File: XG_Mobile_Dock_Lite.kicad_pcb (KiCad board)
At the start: 4 copper layers, 220 x 65 mm, 45 parts, among them J1 5-1775443-8, J10 SWD, J11 UART, J12 I2C1, J13 39300240, J14 469911008, J15 Conn_01x02, J17 8730, J2 20455-040E-76, J3 20455-040E-76, J4 3-2362375-4, J5 USB_C_Receptacle, SW1 SW_Push, U12 STM32F030C8Tx

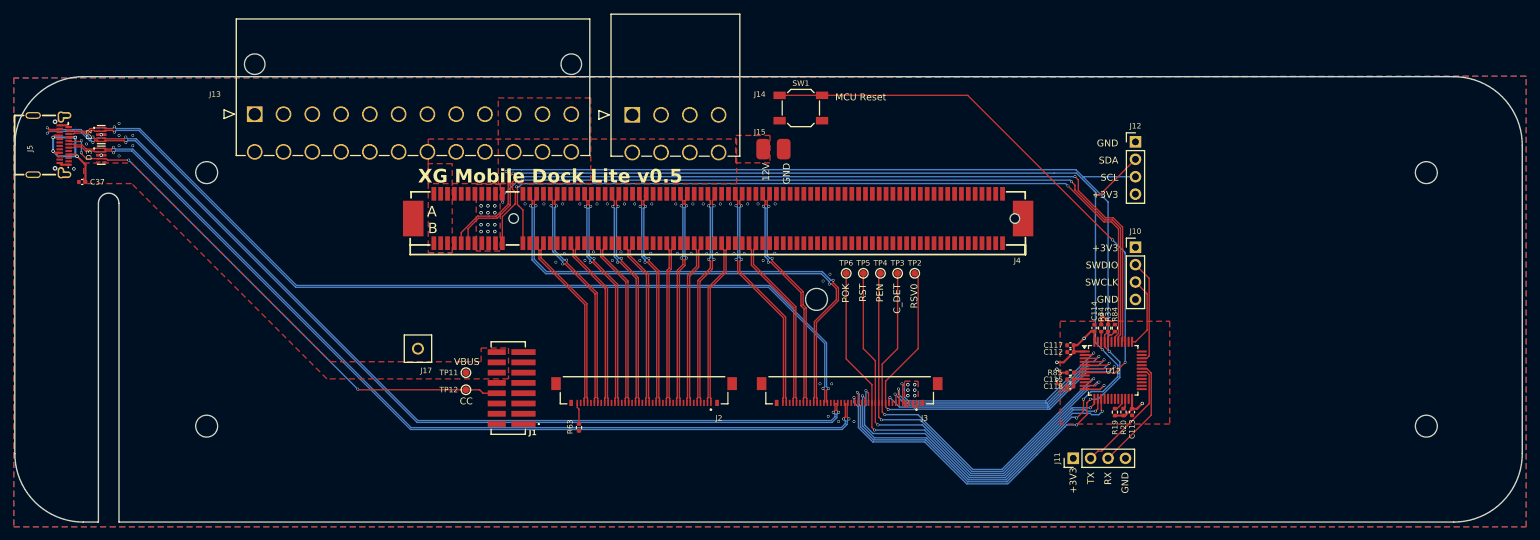
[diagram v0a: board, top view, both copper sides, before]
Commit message: pcb: add pwm fans to lite board
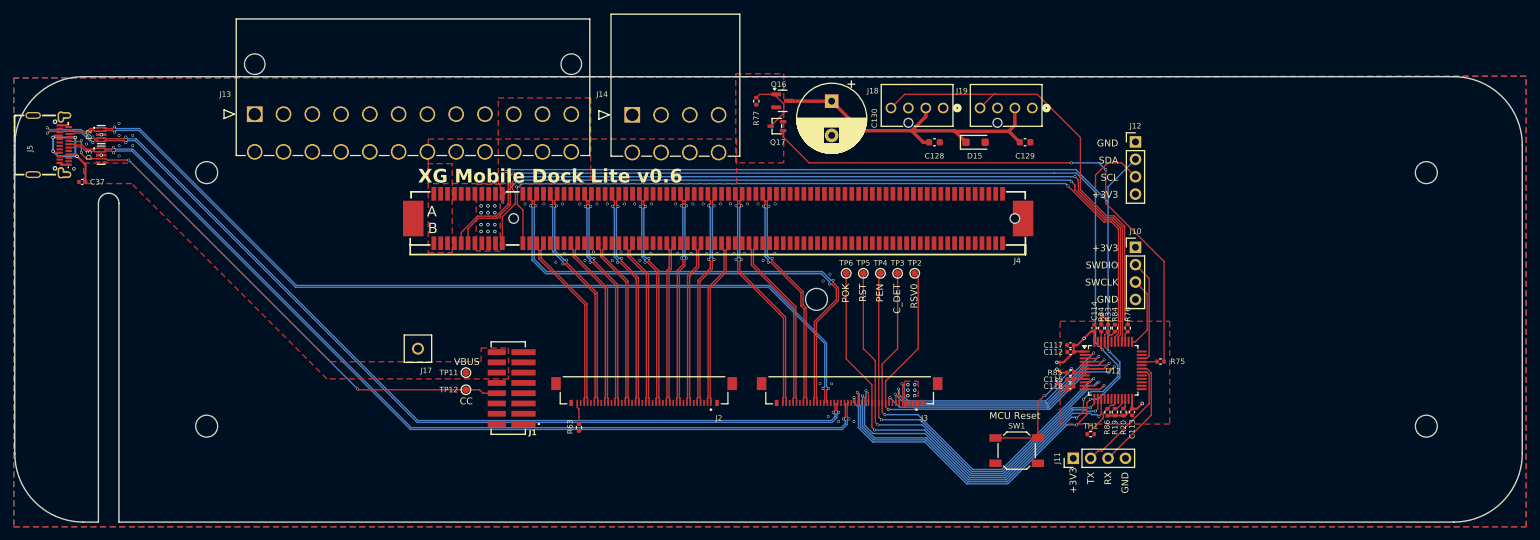
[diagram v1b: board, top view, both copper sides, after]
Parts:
- removed J15: Conn_01x02, XG_Mobile:Solder_Pad_2P
- added C128: 0.1µF, Capacitor_SMD:C_0603_1608Metric, F.Cu at (151.0, 49.0)
- added C129: 0.1µF, Capacitor_SMD:C_0603_1608Metric, F.Cu at (164.2, 49.0)
- added C130: 470µF, Capacitor_THT:CP_Radial_D10.0mm_P5.00mm, F.Cu at (136.0, 43.0)
- added D15: 1N4007, Diode_SMD:D_SOD-123F, F.Cu at (157.0, 49.0)
- added J18: ~, 470531000:CONN_SD-47053-001_H10p00_MOL, F.Cu at (152.3, 44.0)
- added J19: ~, 470531000:CONN_SD-47053-001_H10p00_MOL, F.Cu at (165.3, 44.0)
- added Q16: AO3401A, Package_TO_SOT_SMD:SOT-23, F.Cu at (128.8, 43.0)
- added Q17: 2N7002W, 2N7002W:SOT-323-3_L2.0-W1.3-P1.30-LS2.1-BR, F.Cu at (128.0, 46.6)
- added R75: 100, Resistor_SMD:R_0402_1005Metric, F.Cu at (184.0, 81.0)
- added R76: 330, Resistor_SMD:R_0402_1005Metric, F.Cu at (179.2, 76.1)
- added R77: 10k, Resistor_SMD:R_0402_1005Metric, F.Cu at (125.0, 43.0)
- added R86: 100k, Resistor_SMD:R_0402_1005Metric, F.Cu at (176.2, 88.4)
- added TH1: NCP15WF104F03RC, Resistor_SMD:R_0402_1005Metric, F.Cu at (173.8, 91.6)
- moved SW1 59.1 mm to (163.0, 94.0)
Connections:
- J12 pad 1: GND -> +3V3
- J12 pad 2: /SDA -> /SCL
- J12 pad 3: /SCL -> /SDA
- J12 pad 4: +3V3 -> GND
- U12 pad 16: /SYS_ON -> unconnected-(U12-PA6-Pad16)
- U12 pad 17: /MCU/PA7 -> unconnected-(U12-PA7-Pad17)
- U12 pad 18: /MCU/PB0 -> unconnected-(U12-PB0-Pad18)
- U12 pad 19: unconnected-(U12-PB1-Pad19) -> Net-(U12-PB1)
- U12 pad 20: unconnected-(U12-PB2-Pad20) -> /MCU/PB2
- U12 pad 25: unconnected-(U12-PB12-Pad25) -> /MCU/PB12
- U12 pad 26: unconnected-(U12-PB13-Pad26) -> /MCU/PB13
- U12 pad 27: unconnected-(U12-PB14-Pad27) -> /MCU/PB14
- U12 pad 33: unconnected-(U12-PA12-Pad33) -> /MCU/FAN_ON
- U12 pad 36: unconnected-(U12-PF7-Pad36) -> /MCU/~{CASE_LED}
- U12 pad 39: unconnected-(U12-PB3-Pad39) -> /MCU/FAN_PWM
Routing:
- net Net-(Q17-G): track 0.00 -> 81.5 mm, vias 0 -> 2
- net Net-(J18-Pin_4): track 0.00 -> 65.1 mm
- net /RST_SW: track 84.2 -> 20.9 mm
- net Net-(D15-K): track 0.00 -> 49.8 mm
- net Net-(Q16-G): track 0.00 -> 8.99 mm
- net Net-(U12-PB1): track 0.00 -> 7.05 mm
- net /SDA: track 194.8 -> 197.2 mm
- net /MCU/FAN_ON: track 0.00 -> 2.25 mm
- net /MCU/FAN_PWM: track 0.00 -> 1.64 mm
- net +3V3: track 142.3 -> 143.4 mm
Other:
- board text added: "XG Mobile Dock Lite v0.6"
- board text removed: "12V"
- board text removed: "XG Mobile Dock Lite v0.5"
